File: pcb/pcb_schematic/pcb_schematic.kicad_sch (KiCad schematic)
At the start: 33 parts, among them J1 Conn_ST_STDC14, J3 Conn_02x02_Odd_Even, J4 USB_B_Micro, Q1 MMBT3904, Q2 MMBT3904, Q3 MMBT3904, U1 STM32G031K8Tx, U2 NCP1117-3.3_SOT223, U4 SSD1306 128 x 64 OLED (0x3C), U5 TCS34725 (0x29), Y1 Crystal

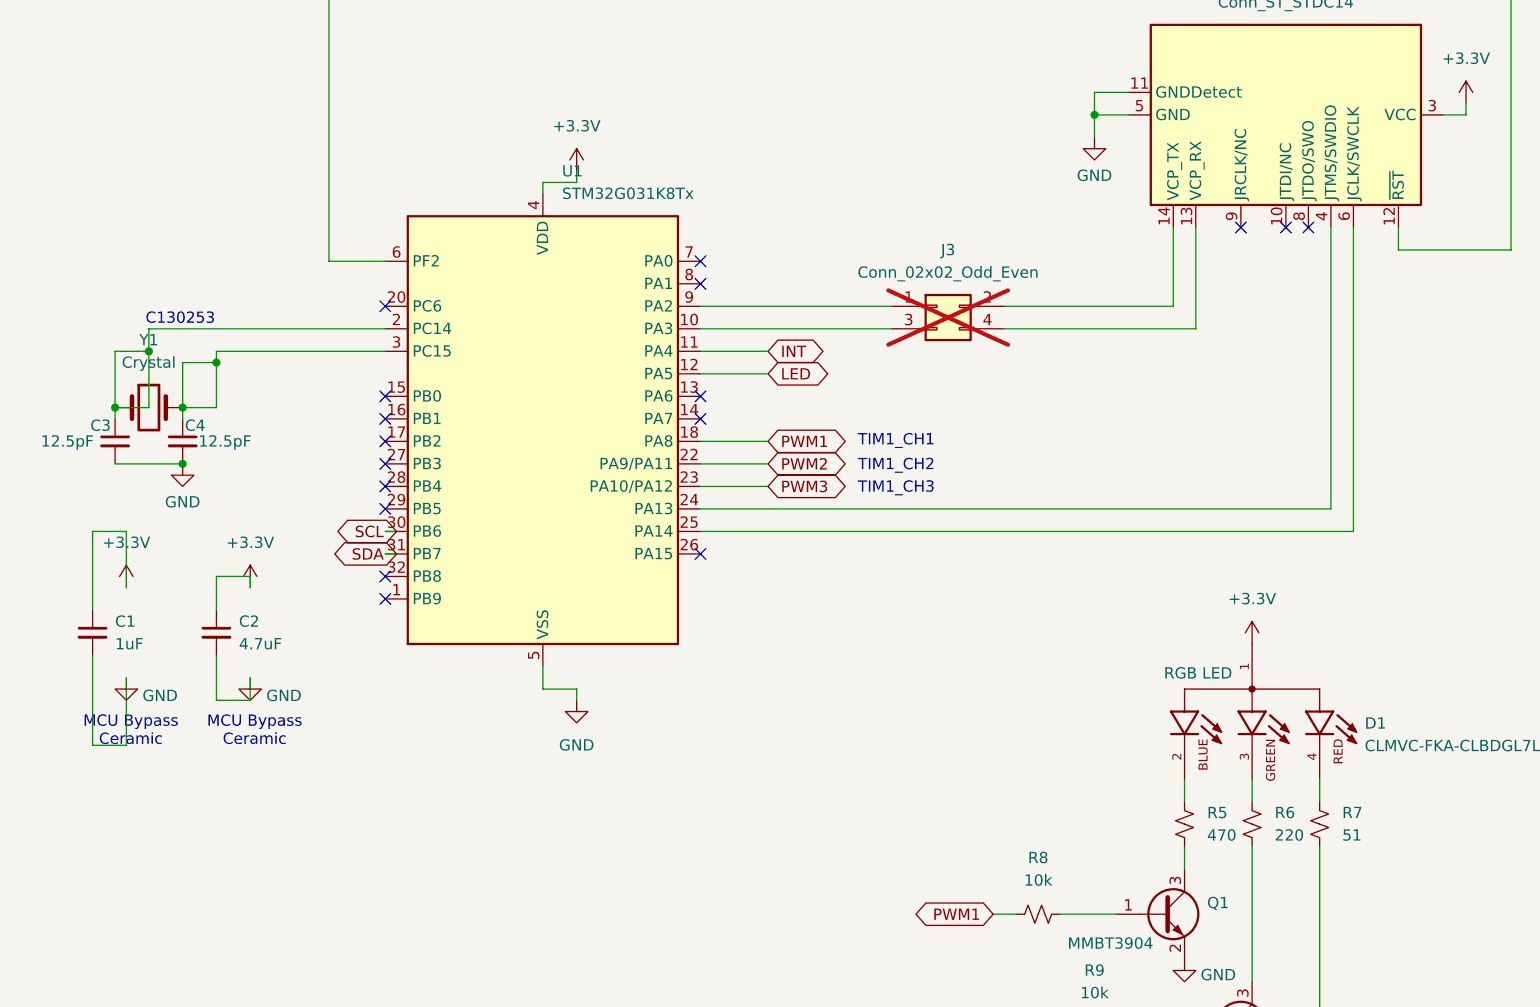
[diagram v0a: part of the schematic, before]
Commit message: Fixed according to feedback
Schematic -> looks like the current limiting resistors for the read and blue LEDs are reversed.

Bypass caps for the MCU are drawn really weird!

Looks like you moved the XTAL and now you have two redundant wires.

PCB -> Identification is in the copper layer, not the silk layer.

C12 does not need vias, the through-hole header serves as vias.

You've got a split on the SDA line of the MCU - try to route from a via, or another pad if you can.

For the power supply, you've not used the filter caps correctly. Go from the USB connector to C8, then to regulator pin 3 (not from reg pin3 to the usb). You can put a fat track between the two pin 2s. You can add a new via size (1mm, 0.8mm) in the via drop-down, and use these vias for punching into the power planes from the caps. The regulator itself should not punch into the power plane, just it's caps should.
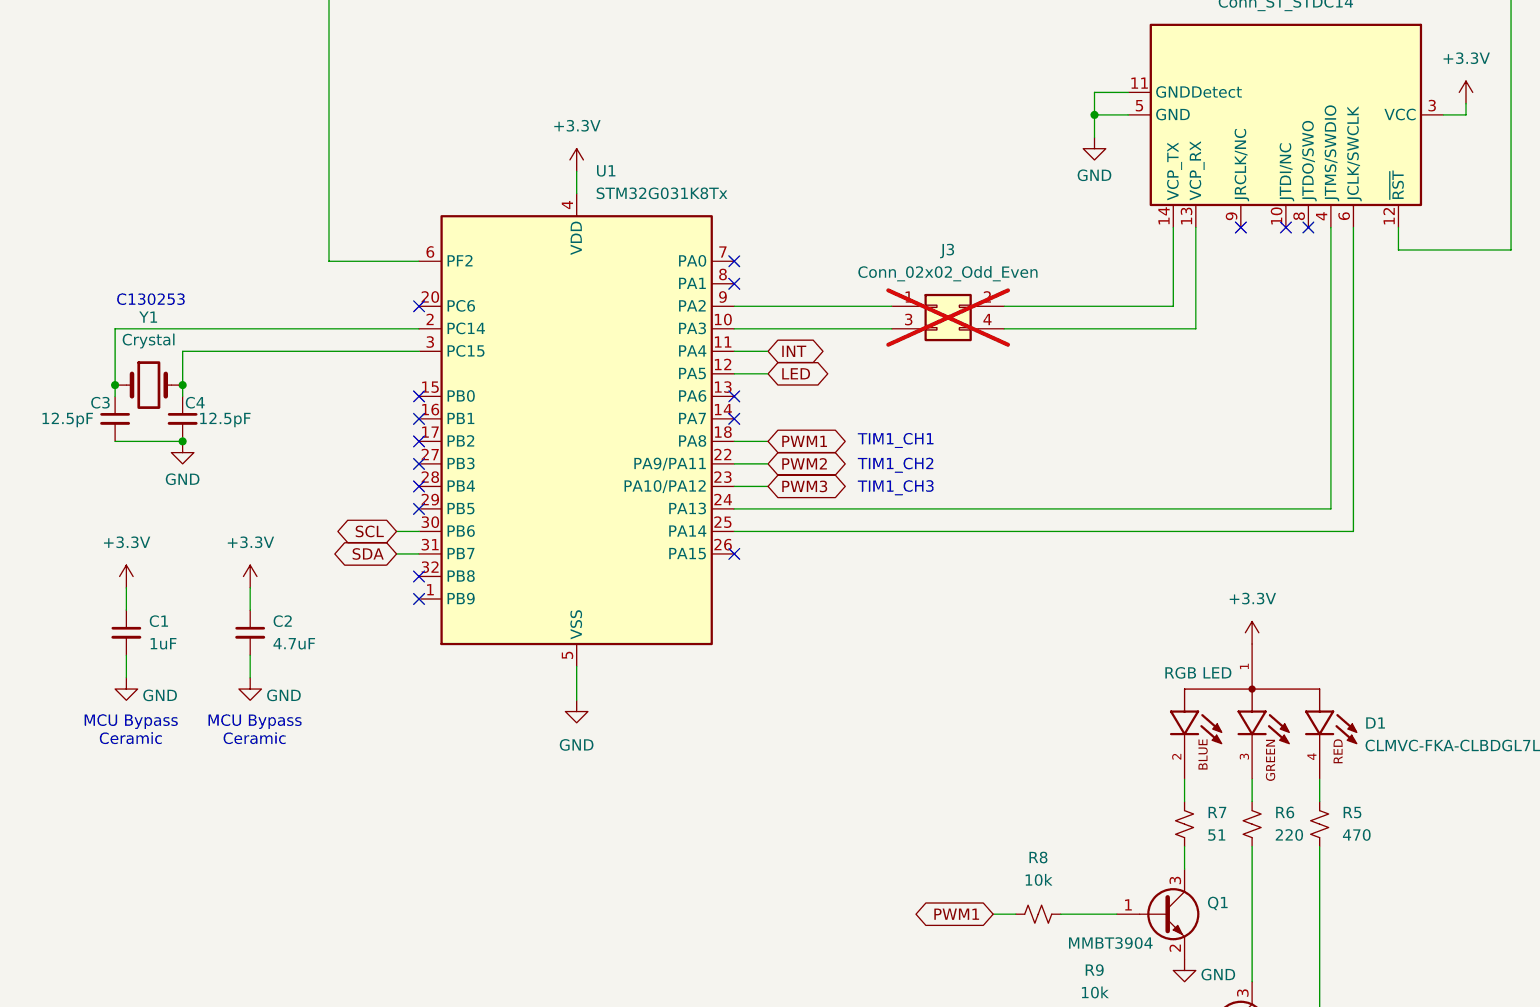
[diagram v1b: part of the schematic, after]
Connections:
- net at R7.1: now also D1.2; no longer D1.4
- net at R7.2: now also Q1.3 (C); no longer Q3.3 (C)
- net at R5.1: now also D1.4; no longer D1.2
- net at R5.2: now also Q3.3 (C); no longer Q1.3 (C)
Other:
- moved on the sheet: C1, C2, C3, C4, R5, R7, U1, Y1
